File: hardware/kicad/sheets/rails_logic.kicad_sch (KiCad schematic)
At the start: 11 parts, among them U6 AP63205WU-7, U7 LD1117S33TR

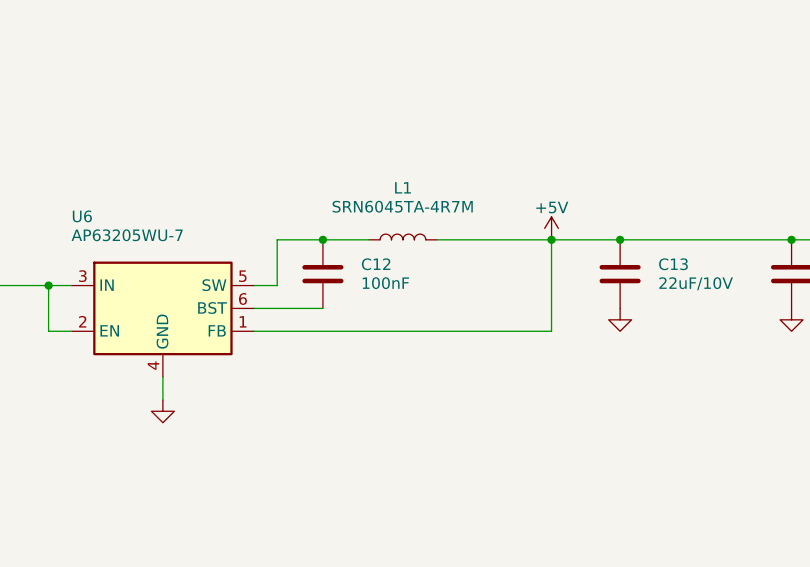
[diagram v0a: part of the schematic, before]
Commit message: KiCad: cleaner layout, decoupling blocks, label directions, KiCad format fixes
- move IC decoupling caps into labelled blocks at the side of each sheet
- global labels show input/output direction per net
- no 4-way junctions (generator now checks and fails)
- generator output matches KiCad's saved format (hide property, junction
  and wire normalisation, lib symbol embedded fonts, multi-unit pins)
- hand-laid USB ESD protection as a pass-through

Co-Authored-By: Claude Sonnet 5.5 <noreply@anthropic.com>
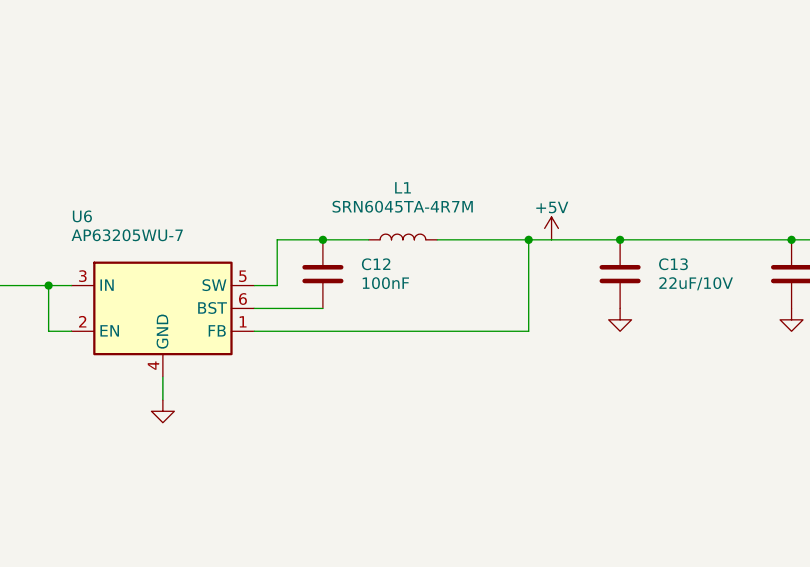
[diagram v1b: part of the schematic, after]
